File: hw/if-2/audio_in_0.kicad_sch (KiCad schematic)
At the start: 31 parts, among them U1 TL072, U2 TL072

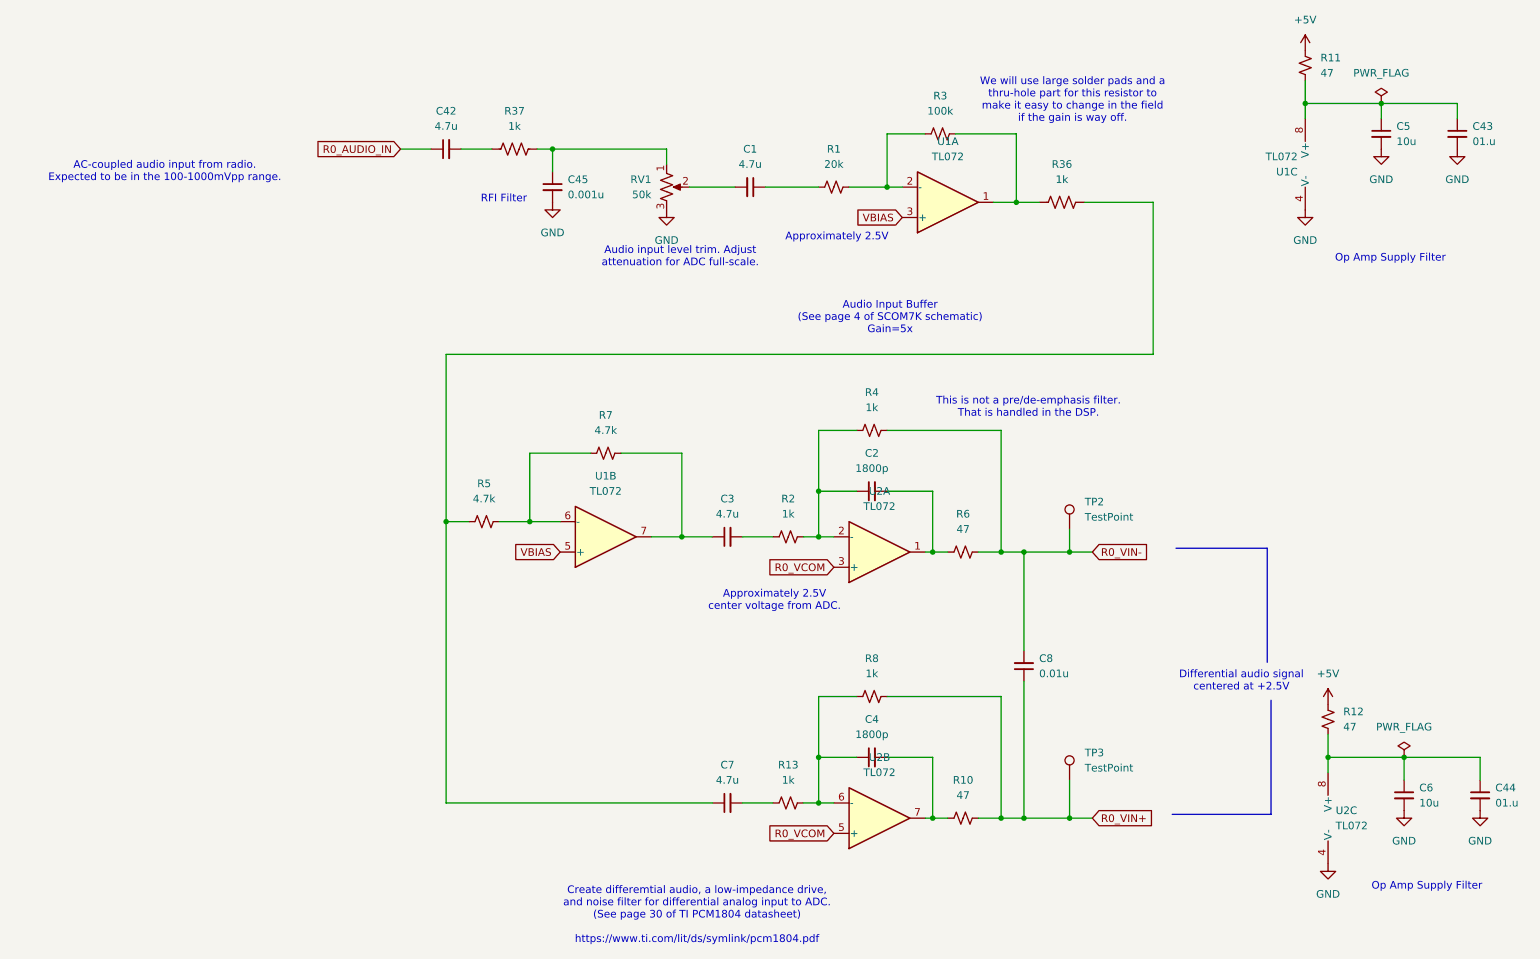
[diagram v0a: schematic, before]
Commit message: Ready to do layout on IF2 board
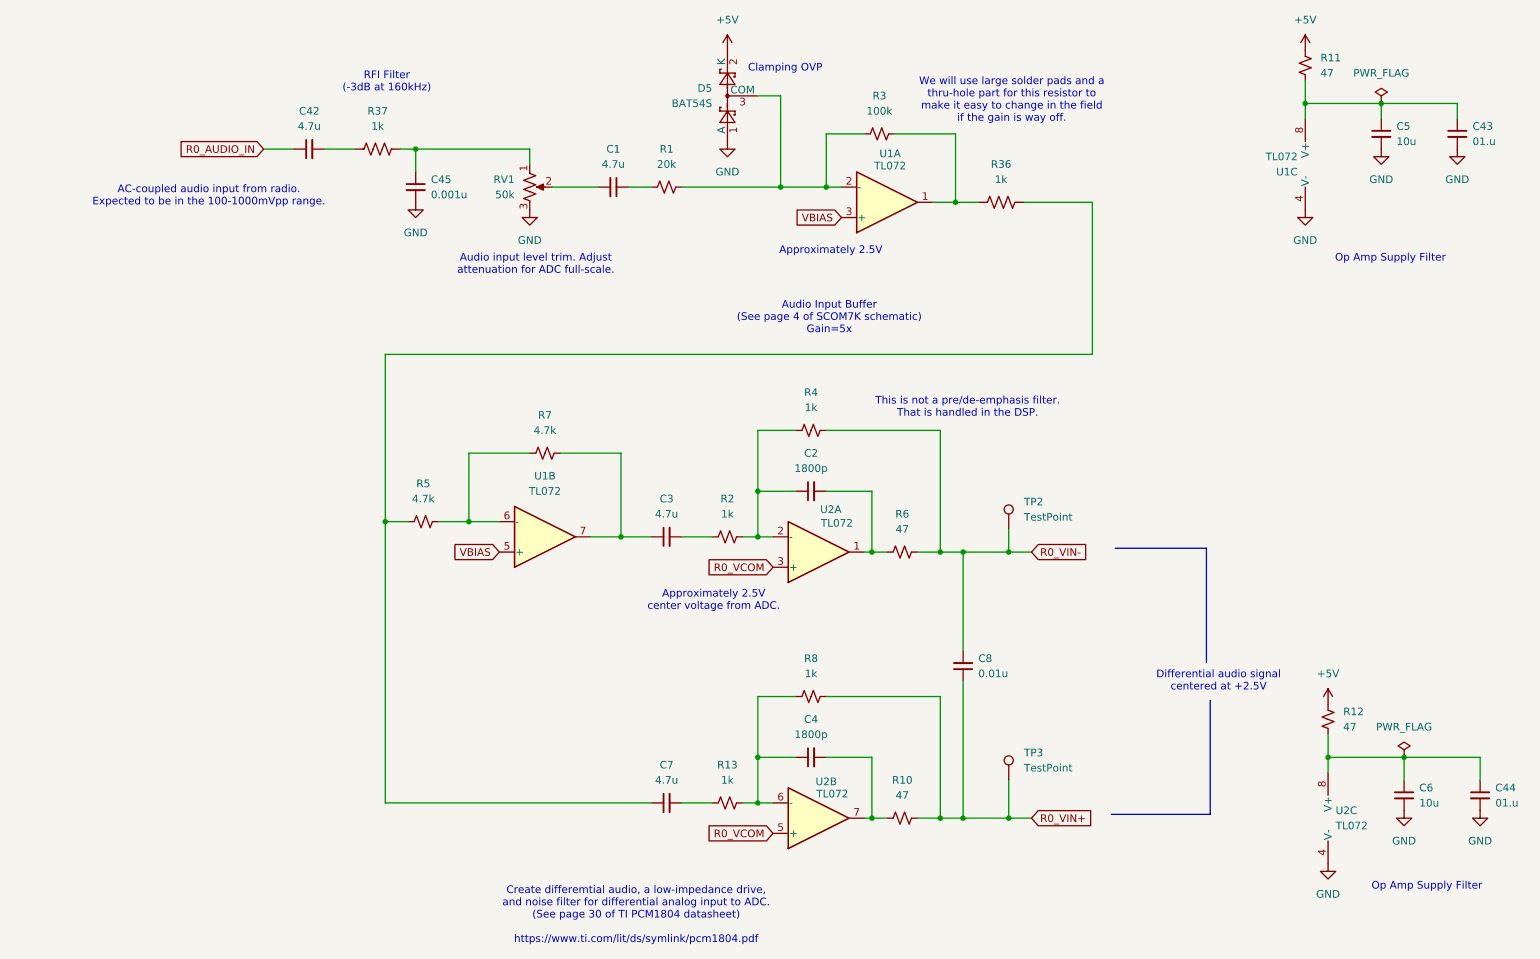
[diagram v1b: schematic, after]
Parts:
- added D5: BAT54S, Package_TO_SOT_SMD:SOT-23, symbol Diode:BAT54S
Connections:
- net +5V: now also D5.2 (K)
- net GND: now also D5.1 (A)
- net at R1.2, R3.1, U1.2 (-): now also D5.3 (COM)
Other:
- note added: "Clamping OVP"
- note added: "RFI Filter (-3dB at 160kHz)"
- note removed: "RFI Filter"
- moved on the sheet: C1, C2, C3, C4, C42, C45, C7, C8, R1, R10, R13, R2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

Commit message: Ready to do layout on IF2 board
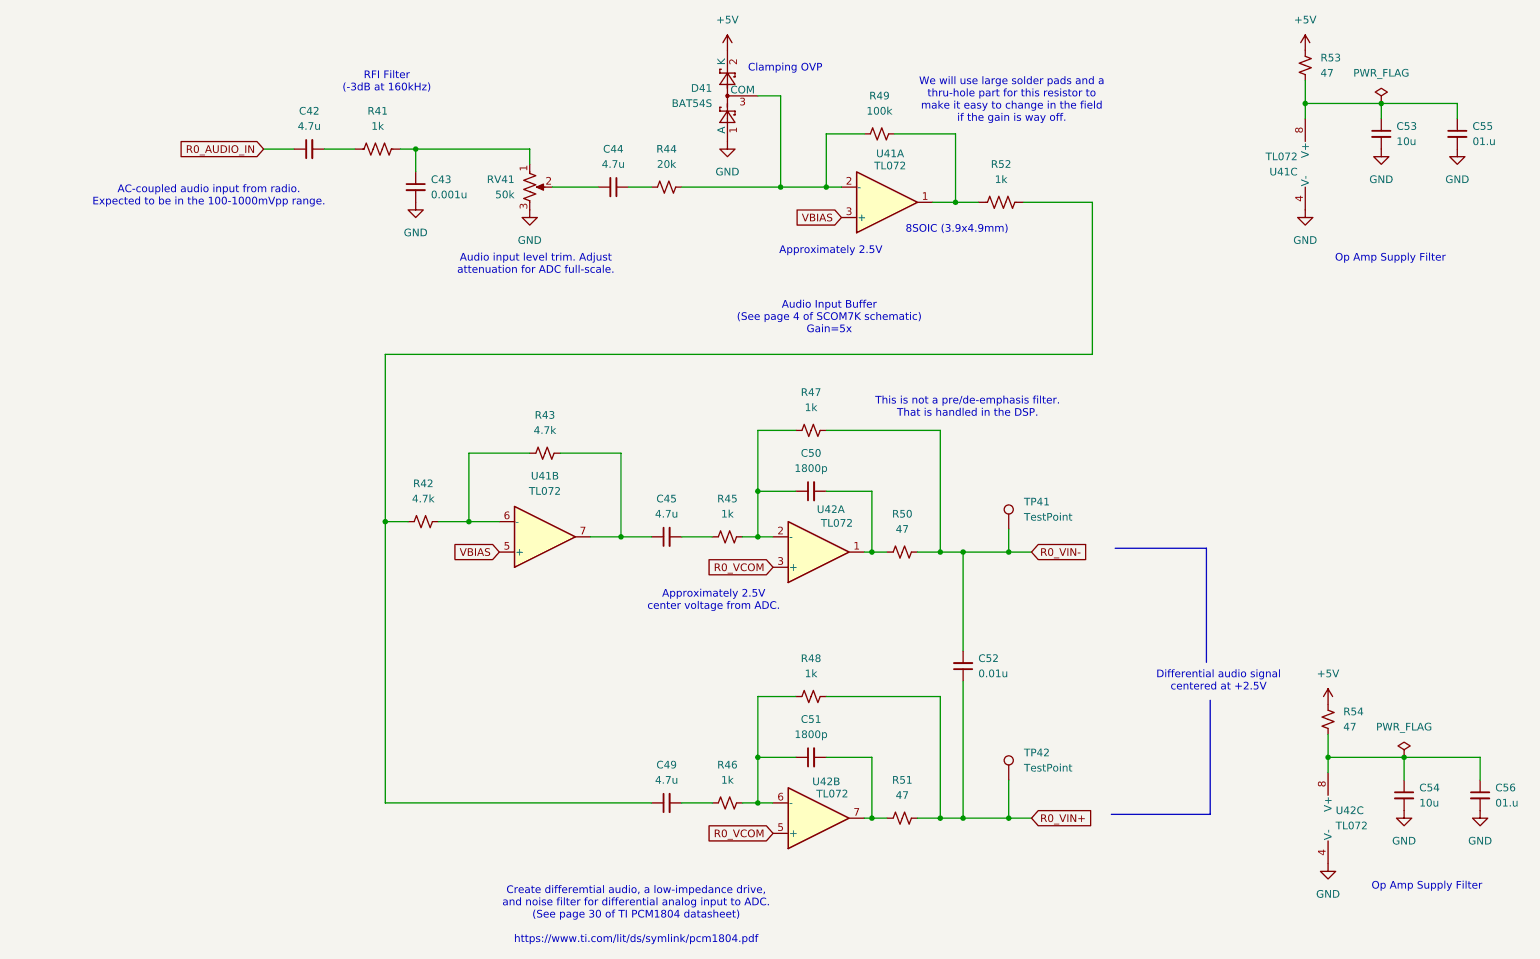
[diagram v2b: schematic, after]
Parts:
- C42: footprint (none) -> Capacitor_SMD:C_0805_2012Metric_Pad1.18x1.45mm_HandSolder
- C43: renamed from C45; footprint (none) -> Capacitor_SMD:C_0805_2012Metric_Pad1.18x1.45mm_HandSolder
- C55: renamed from C43; footprint (none) -> Capacitor_SMD:C_0805_2012Metric_Pad1.18x1.45mm_HandSolder
- C56: renamed from C44; footprint (none) -> Capacitor_SMD:C_0805_2012Metric_Pad1.18x1.45mm_HandSolder
- R41: renamed from R37; footprint (none) -> Resistor_SMD:R_0805_2012Metric_Pad1.20x1.40mm_HandSolder
- R52: renamed from R36; footprint (none) -> Resistor_SMD:R_0805_2012Metric_Pad1.20x1.40mm_HandSolder
- TP41: renamed from TP2; footprint (none) -> TestPoint:TestPoint_Pad_2.5x2.5mm
- TP42: renamed from TP3; footprint (none) -> TestPoint:TestPoint_Pad_2.5x2.5mm
- U41: renamed from U1; footprint (none) -> Package_SO:SOIC-8_3.9x4.9mm_P1.27mm
- U42: renamed from U2; footprint (none) -> Package_SO:SOIC-8_3.9x4.9mm_P1.27mm
- renumbered C1 to C44, C3 to C45, C7 to C49, C2 to C50, C4 to C51, C8 to C52, C5 to C53, C6 to C54, D5 to D41, R5 to R42, R7 to R43, R1 to R44, R2 to R45, R13 to R46, R4 to R47, R8 to R48, R3 to R49, R6 to R50, R10 to R51, R11 to R53, R12 to R54, RV1 to RV41
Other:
- note added: "8SOIC (3.9x4.9mm)"
- title: Audio Input Processing (Radio 0) -> COS/CTCSS/PTT Controls (Radio 1)

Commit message: Making progress on layout
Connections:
- net at R42.1, R52.2: now also C45.1; no longer C49.1
- net at R43.2, U41.7: now also C49.1; no longer C45.1
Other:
- title: COS/CTCSS/PTT Controls (Radio 1) -> COS/CTCSS/PTT Controls (Radio 0)
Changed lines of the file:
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@@
 	(paper "USLetter")
 	(title_block
-		(title "COS/CTCSS/PTT Controls (Radio 1)")
-		(date "2025-03-18")
+		(title "COS/CTCSS/PTT Controls (Radio 0)")
+		(date "2025-05-09")
 		(rev "2")
 		(company "Bruce MacKinnon KC1FSZ")
@@
 	)
 	(junction
+		(at 118.11 73.66)
+		(diameter 0)
+		(color 0 0 0 0)
+	)
+	(junction
 		(at 78.74 39.37)
 		(diameter 0)
@@
 	)
 	(junction
-		(at 73.66 101.6)
-		(diameter 0)
-		(color 0 0 0 0)
-	)
-	(junction
 		(at 177.8 151.13)
 		(diameter 0)
@@
 	(wire
 		(pts
+			(xy 118.11 73.66) (xy 73.66 73.66)
+		)
+		(stroke
+			(width 0)
+			(type default)
+		)
+	)
+	(wire
+		(pts
 			(xy 154.94 151.13) (xy 157.48 151.13)
 		)
@@
 		)
 	)
+	(wire
+		(pts
+			(xy 113.03 148.59) (xy 118.11 148.59)
+		)
+		(stroke
+			(width 0)
+			(type default)
+		)
+	)
 	(polyline
 		(pts
@@
 	(wire
 		(pts
-			(xy 191.77 73.66) (xy 73.66 73.66)
+			(xy 191.77 73.66) (xy 118.11 73.66)
+		)
+		(stroke
+			(width 0)
+			(type default)
+		)
+	)
+	(wire
+		(pts
+			(xy 118.11 73.66) (xy 118.11 104.14)
 		)
 		(stroke
@@
 		)
 	)
-	(wire
-		(pts
-			(xy 113.03 104.14) (xy 118.11 104.14)
-		)
-		(stroke
-			(width 0)
-			(type default)
-		)
-	)
 	(polyline
 		(pts
@@
 	(wire
 		(pts
-			(xy 73.66 101.6) (xy 73.66 148.59)
-		)
-		(stroke
-			(width 0)
-			(type default)
-		)
-	)
-	(wire
-		(pts
 			(xy 135.89 86.36) (xy 135.89 96.52)
 		)
@@
 	(wire
 		(pts
-			(xy 73.66 148.59) (xy 118.11 148.59)
-		)
-		(stroke
-			(width 0)
-			(type default)
-		)
-	)
-	(wire
-		(pts
 			(xy 154.94 106.68) (xy 157.48 106.68)
 		)
@@
 		)
 		(stroke
+			(width 0)
+			(type default)
+		)
+	)
+	(wire
+		(pts
+			(xy 113.03 104.14) (xy 113.03 148.59)
+		)
+		(stroke

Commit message: Making progress on layout
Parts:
- renumbered TP41 to TP2, TP42 to TP3
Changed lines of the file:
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@@
 		(dnp no)
 		(fields_autoplaced yes)
-		(property "Reference" "TP41"
+		(property "Reference" "TP2"
 			(at 180.34 98.2979 0)
 			(effects
@@
 			(project ""
 				(path "/a8c2d6aa-29bb-49bd-a367-0d62a0a32480/a2980c2e-73f3-4531-bb7f-6a925a36f430"
-					(reference "TP41")
+					(reference "TP2")
 					(unit 1)
 				)
@@
 		(dnp no)
 		(fields_autoplaced yes)
-		(property "Reference" "TP42"
+		(property "Reference" "TP3"
 			(at 180.34 140.2079 0)
 			(effects
@@
 			(project "if-2"
 				(path "/a8c2d6aa-29bb-49bd-a367-0d62a0a32480/a2980c2e-73f3-4531-bb7f-6a925a36f430"
-					(reference "TP42")
-					(unit 1)
-				)
+					(reference "TP3")
+					(unit 1)
+				)

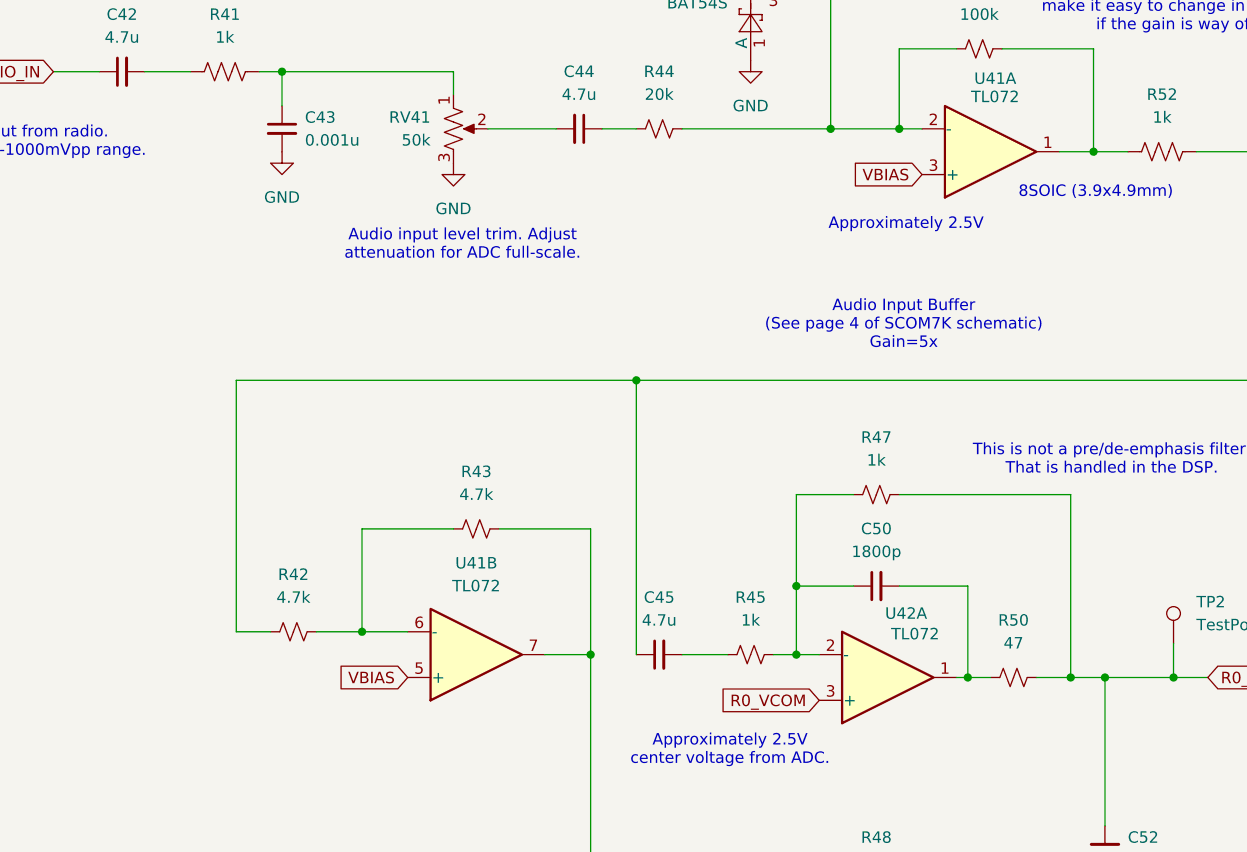
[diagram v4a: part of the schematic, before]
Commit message: (Pre fab) Resolved warning with DB25 shell connections to ground
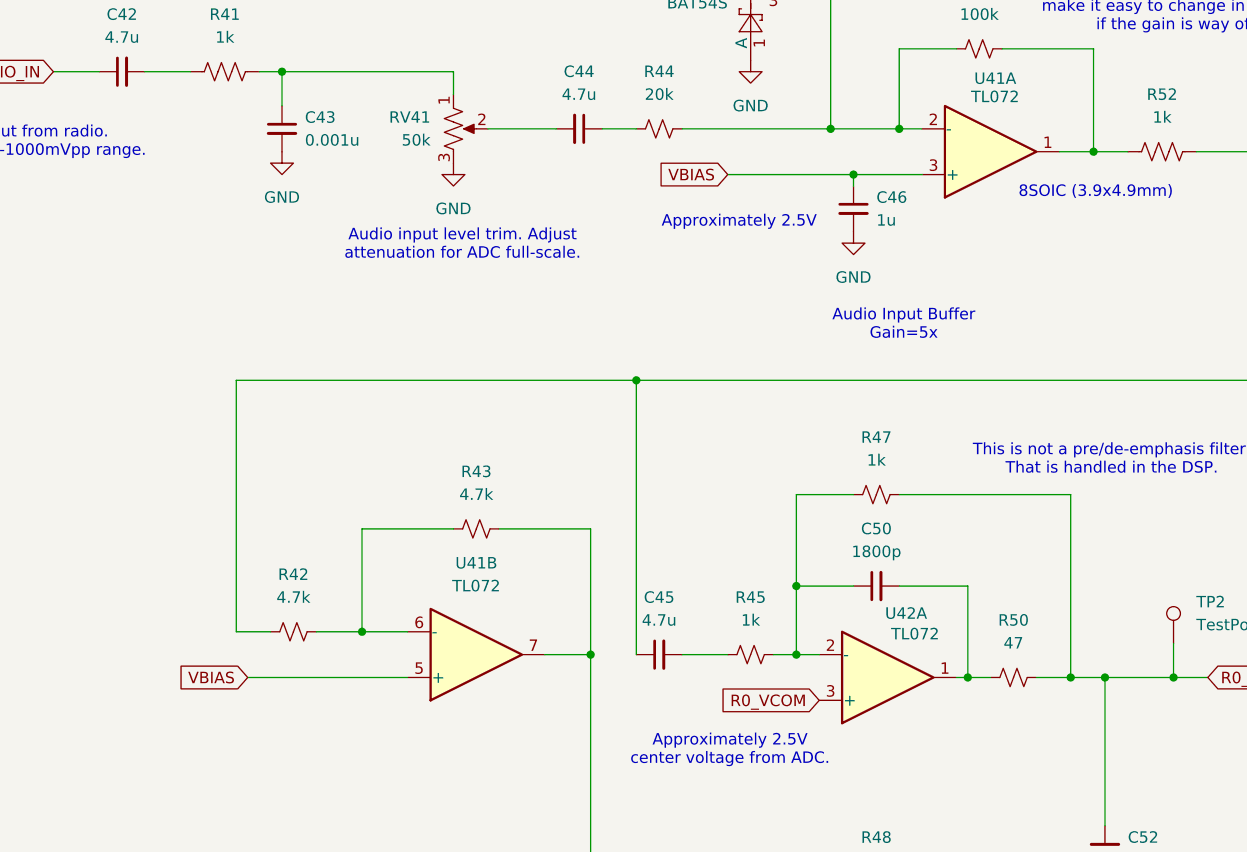
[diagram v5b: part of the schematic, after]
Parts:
- added C46: 1u, Capacitor_SMD:C_0805_2012Metric_Pad1.18x1.45mm_HandSolder, symbol Device:C_Small
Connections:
- net GND: now also C46.2
- net VBIAS: now also C46.1
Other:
- note added: "Audio Input Buffer Gain=5x"
- note removed: "Audio Input Buffer (See page 4 of SCOM7K schematic) Gain=5x"
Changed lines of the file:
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@@
 		)
 	)
-	(text "Audio Input Buffer\n(See page 4 of SCOM7K schematic)\nGain=5x"
+	(text "Audio Input Buffer\nGain=5x"
 		(exclude_from_sim no)
 		(at 147.828 67.564 0)
@@
 	(text "Approximately 2.5V\n"
 		(exclude_from_sim no)
-		(at 148.082 56.388 0)
+		(at 129.54 56.134 0)
 		(effects
 			(font
@@
 	)
 	(junction
+		(at 142.24 50.8)
+		(diameter 0)
+		(color 0 0 0 0)
+	)
+	(junction
 		(at 168.91 48.26)
 		(diameter 0)
@@
 	(wire
 		(pts
+			(xy 142.24 50.8) (xy 142.24 52.07)
+		)
+		(stroke
+			(width 0)
+			(type default)
+		)
+	)
+	(wire
+		(pts
 			(xy 78.74 39.37) (xy 97.79 39.37)
 		)
@@
 	(wire
 		(pts
+			(xy 128.27 50.8) (xy 142.24 50.8)
+		)
+		(stroke
+			(width 0)
+			(type default)
+		)
+	)
+	(wire
+		(pts
 			(xy 153.67 151.13) (xy 154.94 151.13)
 		)
@@
 	(wire
 		(pts
+			(xy 74.93 106.68) (xy 92.71 106.68)
+		)
+		(stroke
+			(width 0)
+			(type default)
+		)
+	)
+	(wire
+		(pts
 			(xy 240.03 34.29) (xy 240.03 31.75)
 		)
@@
 	(wire
 		(pts
+			(xy 142.24 50.8) (xy 149.86 50.8)
+		)
+		(stroke
+			(width 0)
+			(type default)
+		)
+	)
+	(wire
+		(pts
 			(xy 135.89 140.97) (xy 142.24 140.97)
 		)
@@
 	(global_label "VBIAS"
 		(shape input)
-		(at 92.71 106.68 180)
+		(at 74.93 106.68 180)
 		(fields_autoplaced yes)
 		(effects
@@
 		)
 		(property "Intersheetrefs" "${INTERSHEET_REFS}"
-			(at 84.4633 106.68 0)
+			(at 66.6833 106.68 0)
 			(effects
 				(font
@@
 	(global_label "VBIAS"
 		(shape input)
-		(at 149.86 50.8 180)
+		(at 128.27 50.8 180)
 		(fields_autoplaced yes)
 		(effects
@@
 		)
 		(property "Intersheetrefs" "${INTERSHEET_REFS}"
-			(at 141.6133 50.8 0)
+			(at 120.0233 50.8 0)
 			(effects
 				(font
@@
 	)
 	(symbol
+		(lib_id "power:GND")
+		(at 142.24 57.15 0)
+		(unit 1)
+		(exclude_from_sim no)
+		(in_bom yes)
+		(on_board yes)
+		(dnp no)
+		(fields_autoplaced yes)
+		(property "Reference" "#PWR0155"
+			(at 142.24 63.5 0)
+			(effects
+				(font
+					(size 1.27 1.27)
+				)
+				(hide yes)
+			)
+		)
+		(property "Value" "GND"
+			(at 142.24 62.23 0)
+			(effects
+				(font
+					(size 1.27 1.27)
+				)
+			)
+		)
+		(property "Footprint" ""
+			(at 142.24 57.15 0)
+			(effects
+				(font
+					(size 1.27 1.27)
+				)
+				(hide yes)
+			)
+		)
+		(property "Datasheet" ""
+			(at 142.24 57.15 0)
+			(effects
+				(font
+					(size 1.27 1.27)
+				)
+				(hide yes)
+			)
+		)
+		(property "Description" "Power symbol creates a global label with name \"GND\" , ground"
+			(at 142.24 57.15 0)
+			(effects
+				(font
+					(size 1.27 1.27)
+				)
+				(hide yes)
+			)
+		)
+		(pin "1"
+		)
+		(instances
+			(project "if-2"
+				(path "/a8c2d6aa-29bb-49bd-a367-0d62a0a32480/a2980c2e-73f3-4531-bb7f-6a925a36f430"
+					(reference "#PWR0155")
+					(unit 1)
+				)
+			)
+		)
+	)
+	(symbol
 		(lib_id "power:+5V")
 		(at 130.81 22.86 0)
@@
 					(unit 1)
 				)
+			)
+		)
+	)
+	(symbol
+		(lib_id "Device:C_Small")
+		(at 142.24 54.61 0)
+		(unit 1)
+		(exclude_from_sim no)
+		(in_bom yes)
+		(on_board yes)
+		(dnp no)
+		(fields_autoplaced yes)
+		(property "Reference" "C46"
+			(at 144.78 53.3462 0)
+			(effects
+				(font
+					(size 1.27 1.27)
+				)
+				(justify left)
+			)
+		)
+		(property "Value" "1u"
+			(at 144.78 55.8862 0)
+			(effects
+				(font
+					(size 1.27 1.27)
+				)
+				(justify left)
+			)
+		)
+		(property "Footprint" "Capacitor_SMD:C_0805_2012Metric_Pad1.18x1.45mm_HandSolder"
+			(at 142.24 54.61 0)
+			(effects
+				(font
+					(size 1.27 1.27)
+				)
+				(hide yes)
+			)
+		)
+		(property "Datasheet" "~"
+			(at 142.24 54.61 0)
+			(effects
+				(font
+					(size 1.27 1.27)
+				)
+				(hide yes)
+			)
+		)
+		(property "Description" "Unpolarized capacitor, small symbol"
+			(at 142.24 54.61 0)
+			(effects
+				(font
+					(size 1.27 1.27)
+				)
+				(hide yes)
+			)
+		)
+		(pin "1"
+		)
+		(pin "2"
+		)
+		(instances
+			(project "if-2"
+				(path "/a8c2d6aa-29bb-49bd-a367-0d62a0a32480/a2980c2e-73f3-4531-bb7f-6a925a36f430"
+					(reference "C46")
+					(unit 1)
+				)
